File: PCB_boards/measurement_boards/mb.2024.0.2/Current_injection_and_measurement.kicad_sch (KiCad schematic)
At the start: 23 parts, among them J12 Conn_01x08_Female, J14 Conn_01x02_Female, J15 Conn_01x08_Female, J20 shunt +, J21 shunt -, K3 G5LE-1, K4 G5LE-1, K5 G5LE-1, K6 G5LE-1, Q3 ZVN4206ASTZ, Q4 ZVN4206ASTZ, Q5 ZVN4206ASTZ, Q6 ZVN4206ASTZ, U5 1085

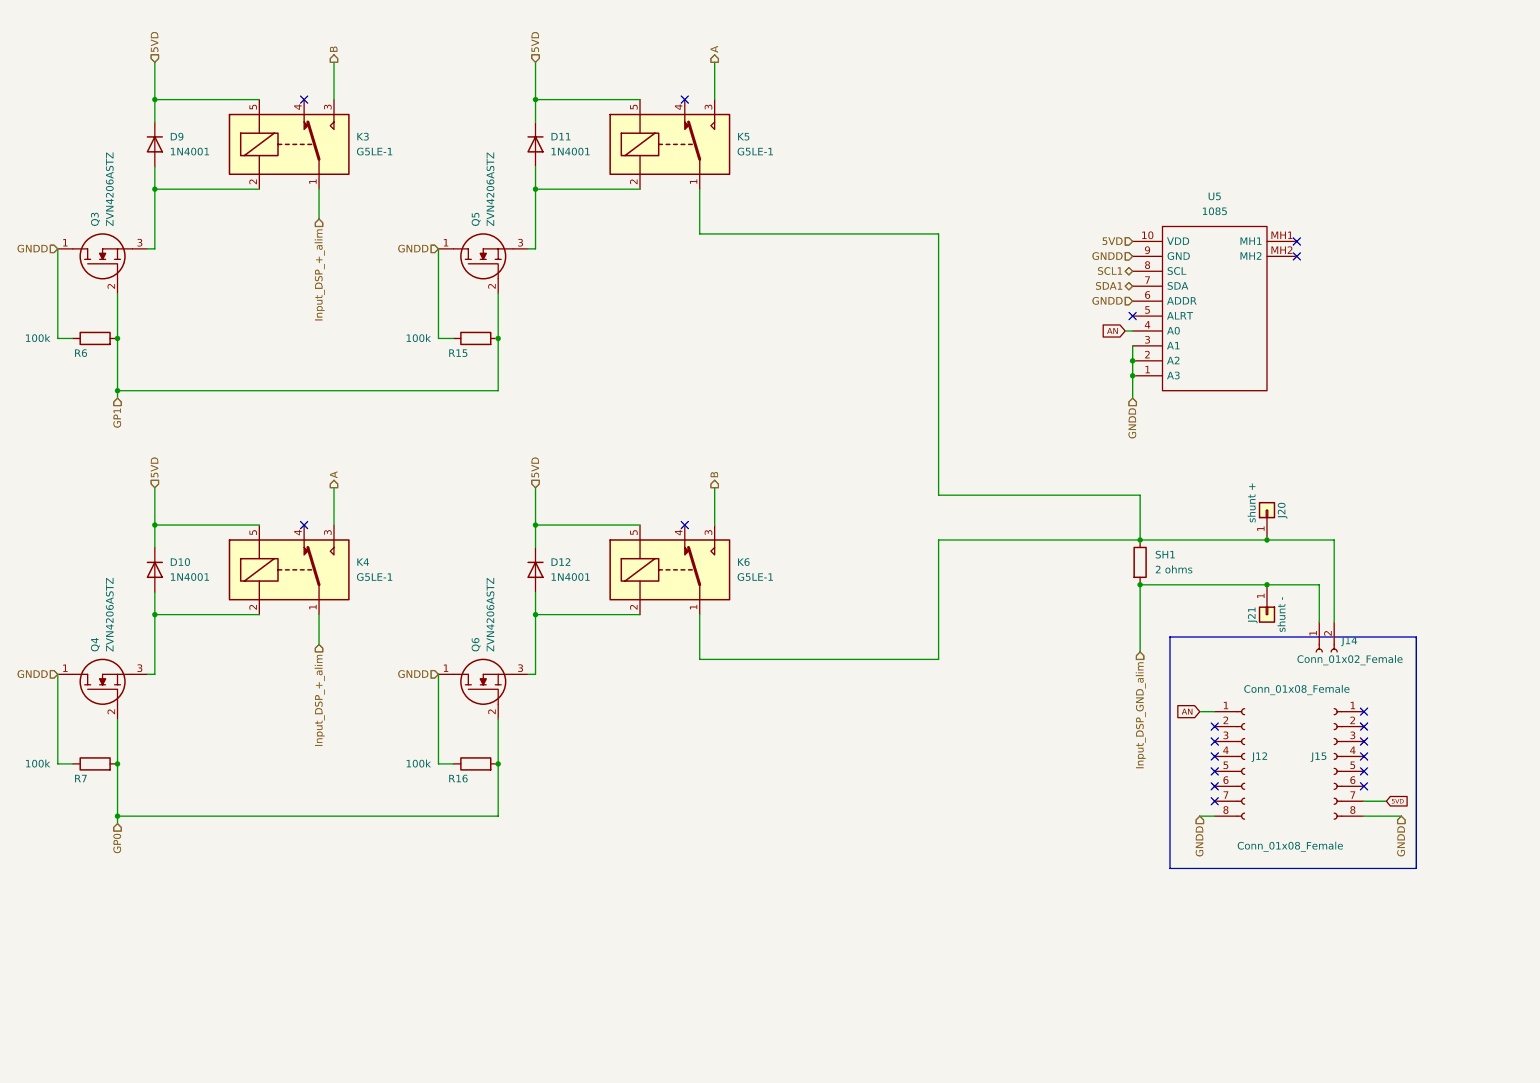
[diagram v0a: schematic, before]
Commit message: correction DPS, add dischage resistor, remove 63 warning on the schemtic, remove 7 errors in schematics change resistor designation, update pcb
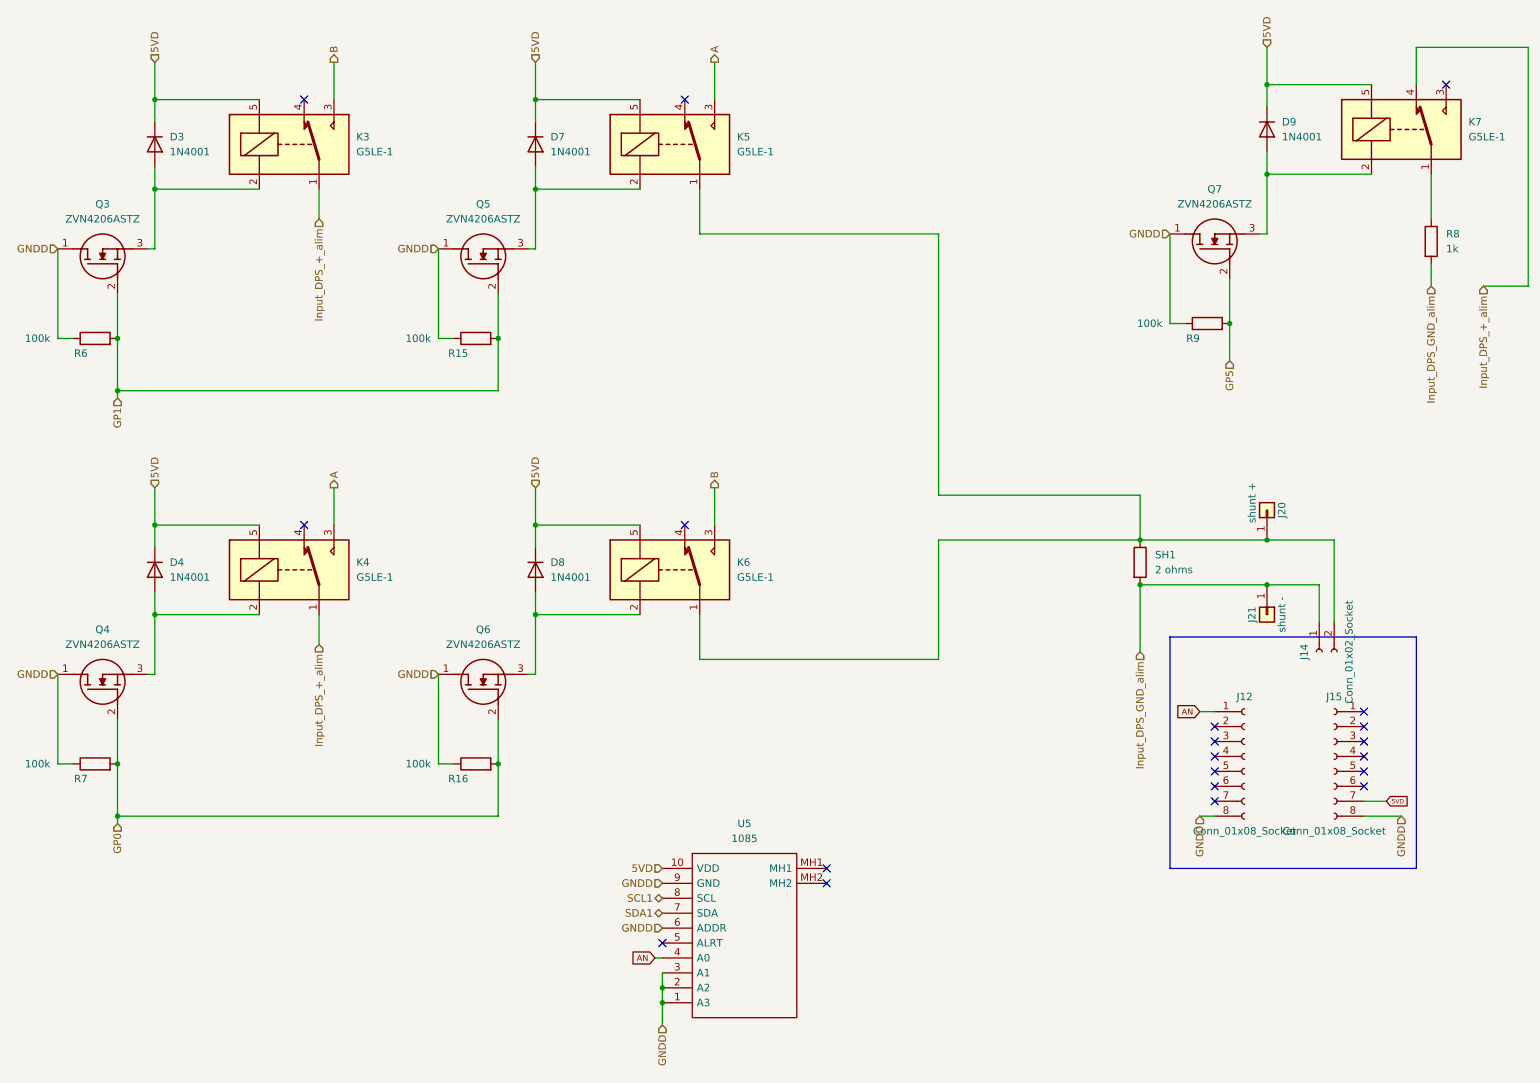
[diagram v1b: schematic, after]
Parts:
- added D9: 1N4001, Diode_THT:D_DO-41_SOD81_P10.16mm_Horizontal, symbol Diode:1N4001
- added K7: G5LE-1, Relay_THT:Relay_SPDT_Omron-G5LE-1, symbol Relay:G5LE-1
- added Q7: ZVN4206ASTZ, Package_TO_SOT_THT:TO-92L_Wide, symbol ZVN4206ASTZ:ZVN4206ASTZ
- added R8: 1k, Resistor_THT:R_Axial_DIN0207_L6.3mm_D2.5mm_P7.62mm_Horizontal, symbol Device:R
- added R9: 100k, Resistor_THT:R_Axial_DIN0207_L6.3mm_D2.5mm_P7.62mm_Horizontal, symbol Device:R
- J12, J15: value Conn_01x08_Female -> Conn_01x08_Socket; symbol Connector:Conn_01x08_Female -> Connector:Conn_01x08_Socket
- J14: value Conn_01x02_Female -> Conn_01x02_Socket; symbol Connector:Conn_01x02_Female -> Connector:Conn_01x02_Socket
- Q3, Q4, Q5, Q6: symbol ZVN4206A:ZVN4206ASTZ -> ZVN4206ASTZ:ZVN4206ASTZ; Manufacturer_Name Diodes Inc. -> Diodes Incorporated
- renumbered D9 to D3, D10 to D4, D11 to D7, D12 to D8
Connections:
- net 5VD: now also D9.1 (K), K7.5
- net GNDD: now also Q7.1 (D), R9.1
- net Input_DSP_+_alim renamed Input_DPS_+_alim
- net Input_DPS_+_alim: now also K7.4
- net Input_DSP_GND_alim renamed Input_DPS_GND_alim
- net Input_DPS_GND_alim: now also R8.2
- new net: K7.1, R8.1
- new net: D9.2 (A), K7.2, Q7.3 (S)
- new net GP5: Q7.2 (G), R9.2
- no-connect marks 19 -> 20
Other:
- moved on the sheet: U5
